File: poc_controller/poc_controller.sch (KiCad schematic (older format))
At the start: 19 parts, among them J1 CONN_01X06, J2 CONN_01X06, J3 CONN_01X02, J4 CONN_01X02, J5 CONN_01X02, SW1 SW_DPST, U1 dsPIC33EPXXXMC502, Y1 Crystal

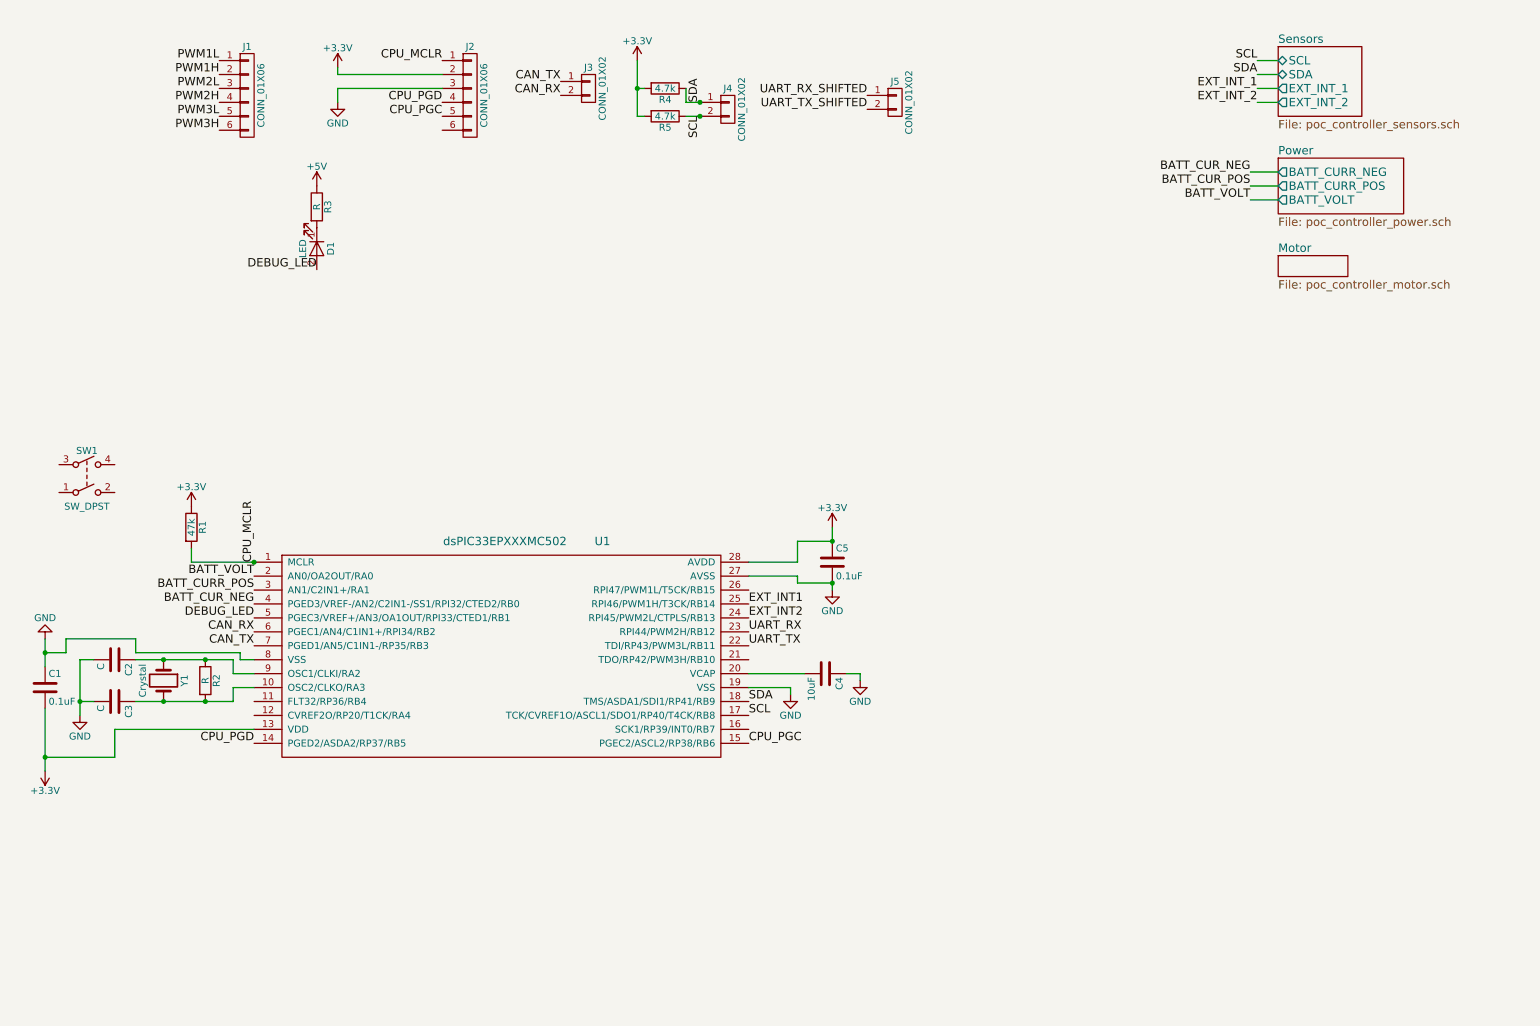
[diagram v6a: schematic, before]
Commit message: Add UART level shifting.
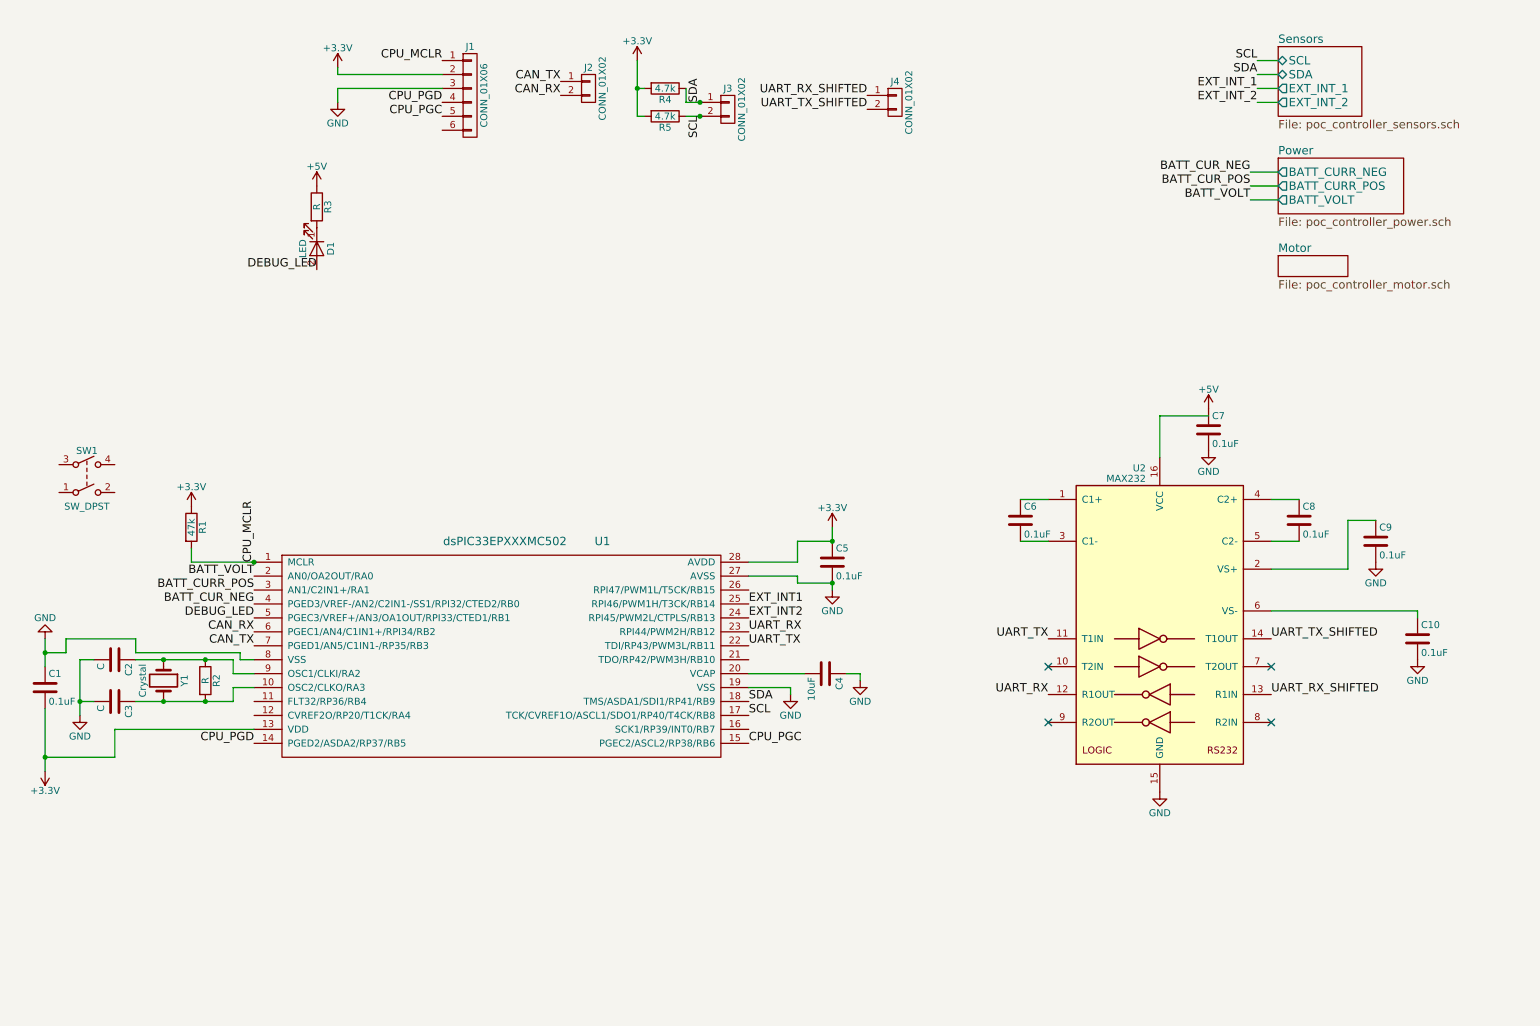
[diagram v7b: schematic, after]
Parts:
- removed J1: CONN_01X06, Pin_Headers:Pin_Header_Straight_1x06_Pitch2.54mm, symbol CONN_01X06
- added C10, C6, C7, C8, C9: 0.1uF, Capacitors_SMD:C_1206_HandSoldering, symbol C
- added U2: MAX232, Housings_SOIC:SOIC-16_3.9x9.9mm_Pitch1.27mm, symbol MAX232
- renumbered J2 to J1, J3 to J2, J4 to J3, J5 to J4
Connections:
- net +5V: now also C7.1
- net GND: now also C10.2, C7.2, C9.2, U2.15 (GND)
- net UART_RX: now also U2.12 (R1OUT)
- net UART_RX_SHIFTED: now also U2.13 (R1IN)
- net UART_TX: now also U2.11 (T1IN)
- net UART_TX_SHIFTED: now also U2.14 (T1OUT)
- new net: C6.1, U2.1 (C1+)
- new net: C9.1, U2.2 (VS+)
- new net: C6.2, U2.3 (C1-)
- new net: C8.1, U2.4 (C2+)
- new net: C8.2, U2.5 (C2-)
- new net: C10.1, U2.6 (VS-)
- no-connect marks 0 -> 4

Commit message: Debug LED
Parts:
- D1: footprint (none) -> LEDs:LED_1206_HandSoldering; Part Number (none) -> 160-1643-1-ND
- R3: value R -> 100; footprint (none) -> Resistors_SMD:R_1206_HandSoldering; Part Number (none) -> 311-100FRCT-ND
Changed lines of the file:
@@
 P 2700 1800
 F 0 "R3" V 2780 1800 50  0000 C CNN
-F 1 "R" V 2700 1800 50  0000 C CNN
-F 2 "" V 2630 1800 50  0001 C CNN
+F 1 "100" V 2700 1800 50  0000 C CNN
+F 2 "Resistors_SMD:R_1206_HandSoldering" V 2630 1800 50  0001 C CNN
 F 3 "" H 2700 1800 50  0001 C CNN
+F 4 "311-100FRCT-ND" V 2700 1800 60  0001 C CNN "Part Number"
 	1    2700 1800
 	1    0    0    -1
@@
 F 0 "D1" H 2700 2200 50  0000 C CNN
 F 1 "LED" H 2700 2000 50  0000 C CNN
-F 2 "" H 2700 2100 50  0001 C CNN
+F 2 "LEDs:LED_1206_HandSoldering" H 2700 2100 50  0001 C CNN
 F 3 "" H 2700 2100 50  0001 C CNN
+F 4 "160-1643-1-ND" H 2700 2100 60  0001 C CNN "Part Number"
 	1    2700 2100
 	0    1    1    0
